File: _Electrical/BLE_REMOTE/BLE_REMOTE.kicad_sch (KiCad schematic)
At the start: 4 parts

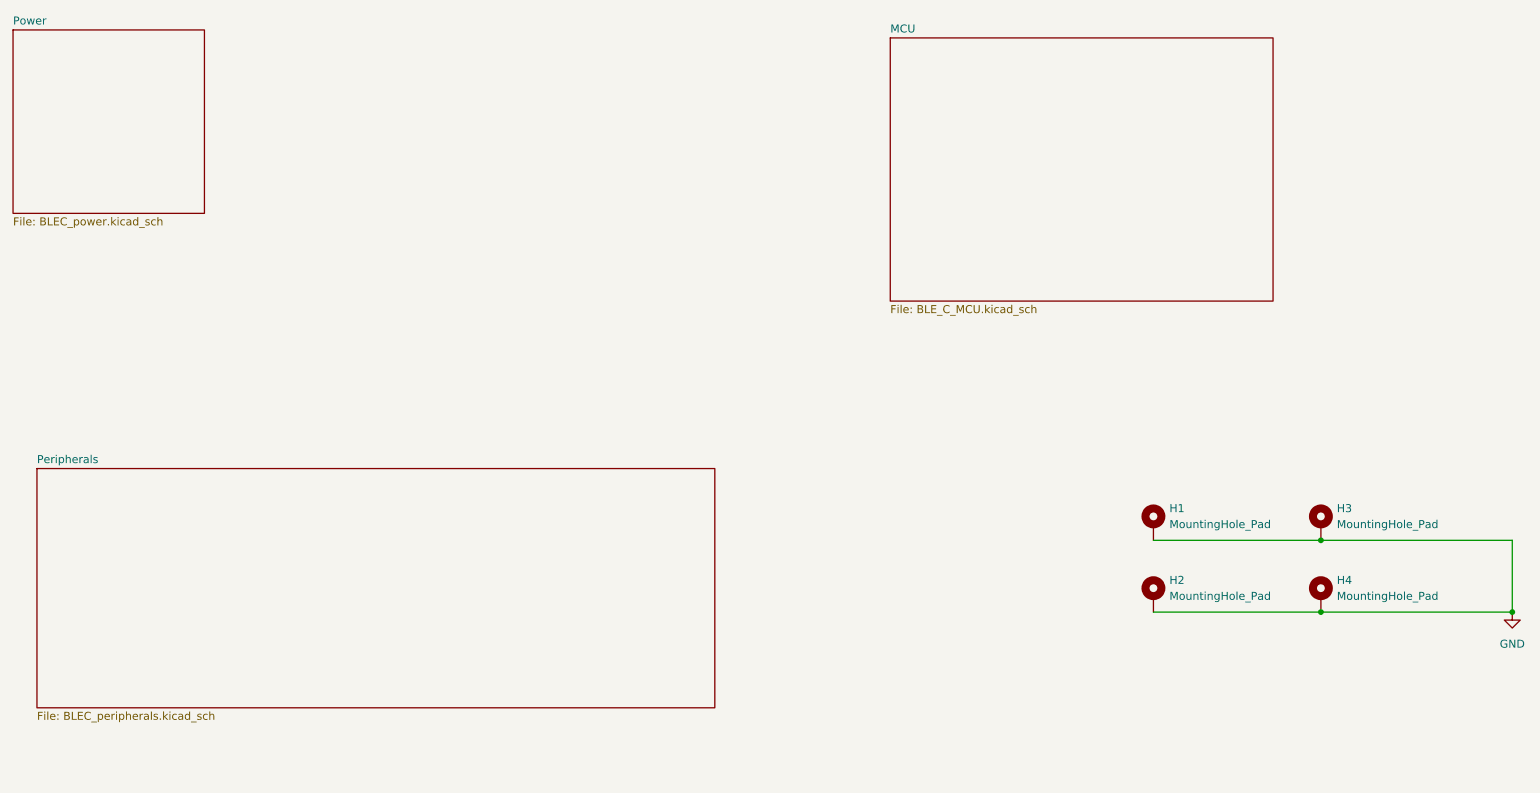
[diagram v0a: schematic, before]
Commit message: Added simulation and updated power button
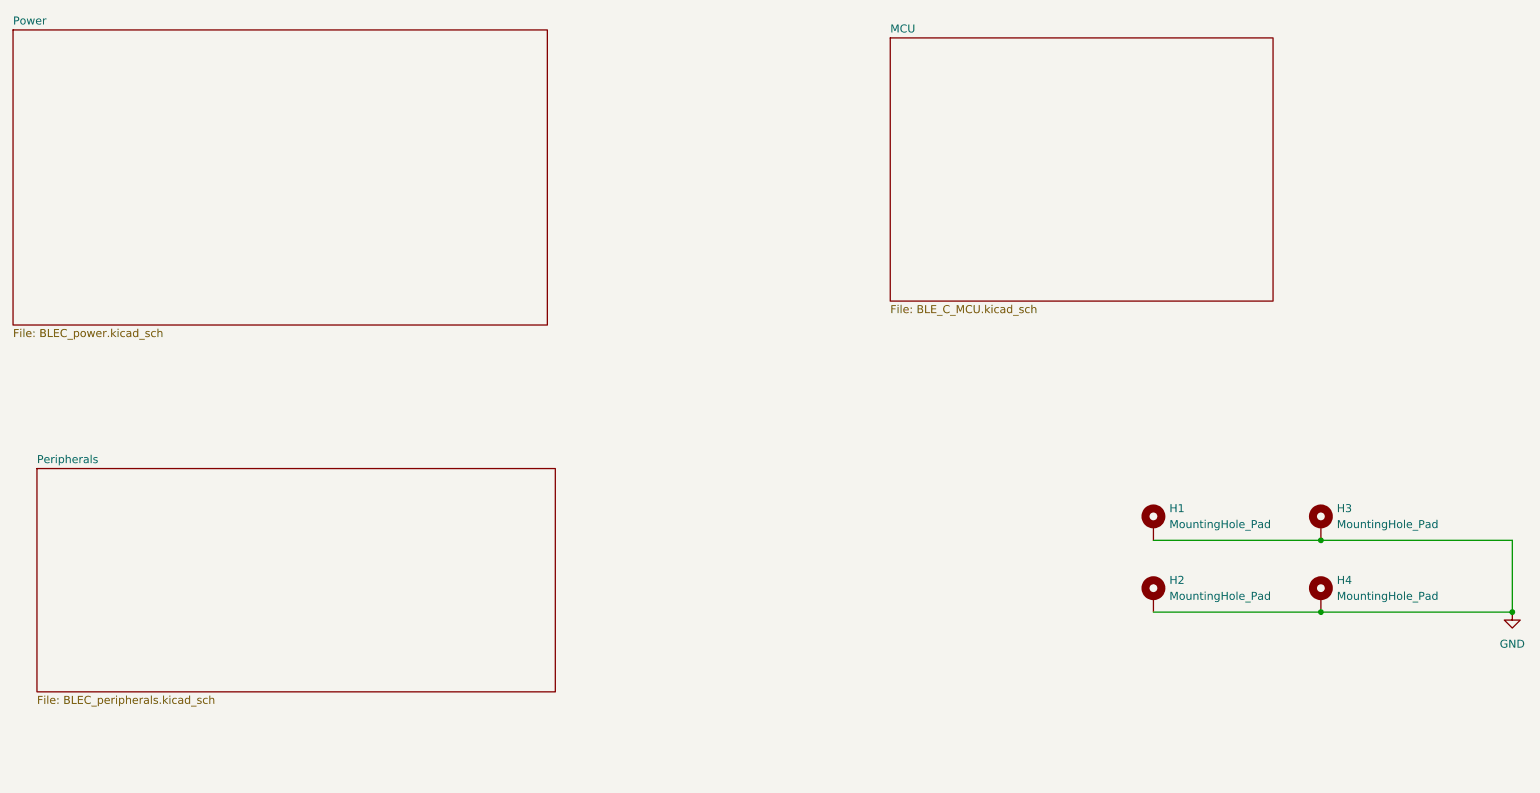
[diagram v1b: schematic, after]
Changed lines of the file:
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@@
     )
   )
-  (sheet (at 34.29 110.49) (size 107.95 38.1) (fields_autoplaced)
+  (sheet (at 34.29 110.49) (size 82.55 35.56) (fields_autoplaced)
     (stroke (width 0.1524) (type solid))
     (fill (color 0 0 0 0.0000))
@@
       (effects (font (size 1.27 1.27)) (justify left bottom))
     )
-    (property "Sheetfile" "BLEC_peripherals.kicad_sch" (at 34.29 149.1746 0)
+    (property "Sheetfile" "BLEC_peripherals.kicad_sch" (at 34.29 146.6346 0)
       (effects (font (size 1.27 1.27)) (justify left top))
     )
@@
     )
   )
-  (sheet (at 30.48 40.64) (size 30.48 29.21) (fields_autoplaced)
+  (sheet (at 30.48 40.64) (size 85.09 46.99) (fields_autoplaced)
     (stroke (width 0.1524) (type solid))
     (fill (color 0 0 0 0.0000))
@@
       (effects (font (size 1.27 1.27)) (justify left bottom))
     )
-    (property "Sheetfile" "BLEC_power.kicad_sch" (at 30.48 70.4346 0)
+    (property "Sheetfile" "BLEC_power.kicad_sch" (at 30.48 88.2146 0)
       (effects (font (size 1.27 1.27)) (justify left top))
     )

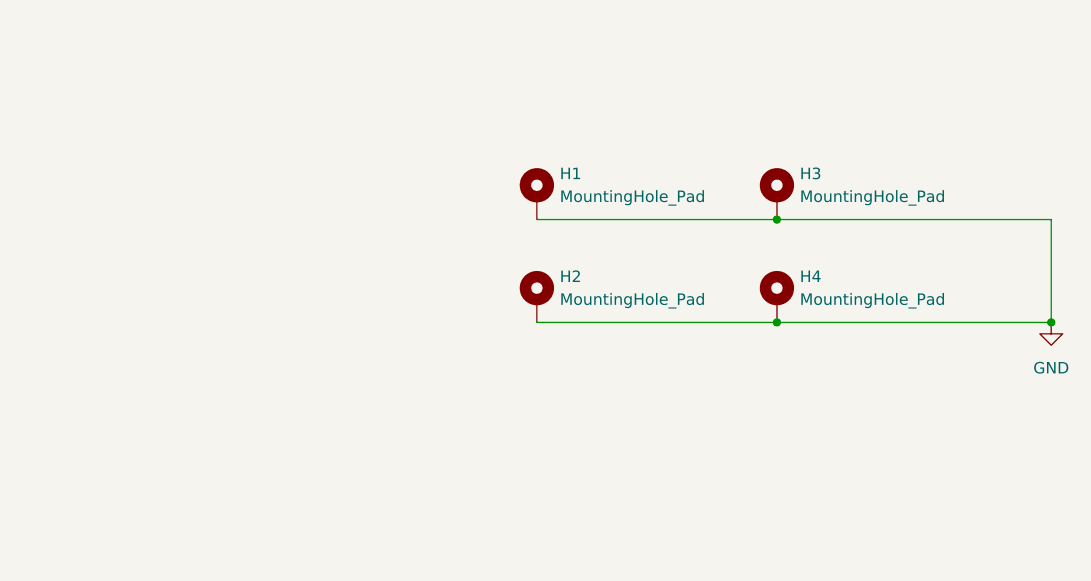
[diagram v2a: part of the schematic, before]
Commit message: Finished initial PCB draft
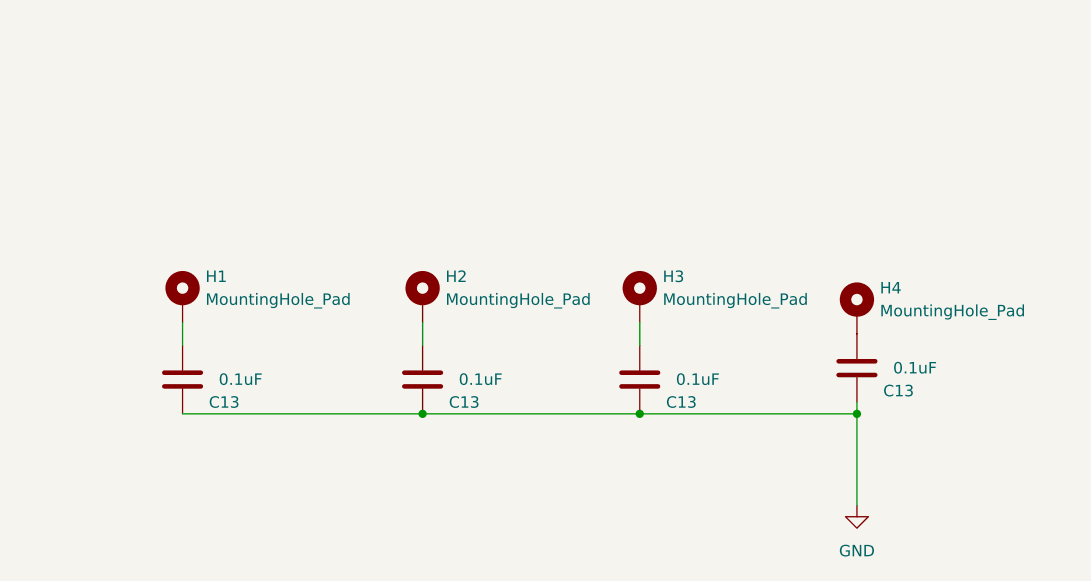
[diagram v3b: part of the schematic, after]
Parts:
- added C13 (x4): 0.1uF, Capacitor_SMD:C_0402_1005Metric_Pad0.74x0.62mm_HandSolder, symbol Device:C
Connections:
- net GND: now also C13.1, C13.1, C13.1, C13.1; no longer H1.1, H2.1, H3.1, H4.1
- new net: C13.2, H4.1
- new net: C13.2, H2.1
- new net: C13.2, H1.1
- new net: C13.2, H3.1
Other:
- moved on the sheet: H1, H2, H3, H4

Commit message: asdasat
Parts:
- removed C13 (x4): 0.1uF, Capacitor_SMD:C_0402_1005Metric_Pad0.74x0.62mm_HandSolder, symbol Device:C
- added R25 (x4): 0R, Resistor_SMD:R_0402_1005Metric_Pad0.72x0.64mm_HandSolder, symbol Device:R
- H1, H2, H3, H4: now left out of the parts list
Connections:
- net GND: now also R25.2, R25.2, R25.2, R25.2
- net at H4.1: now also R25.1
- net at H2.1: now also R25.1
- net at H1.1: now also R25.1
- net at H3.1: now also R25.1
